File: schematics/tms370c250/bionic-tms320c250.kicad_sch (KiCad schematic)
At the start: 10 parts, among them J1 Bionic-P135, J2 Bionic-P245, U1 TMS370C250, U2 11AA010-I/TT

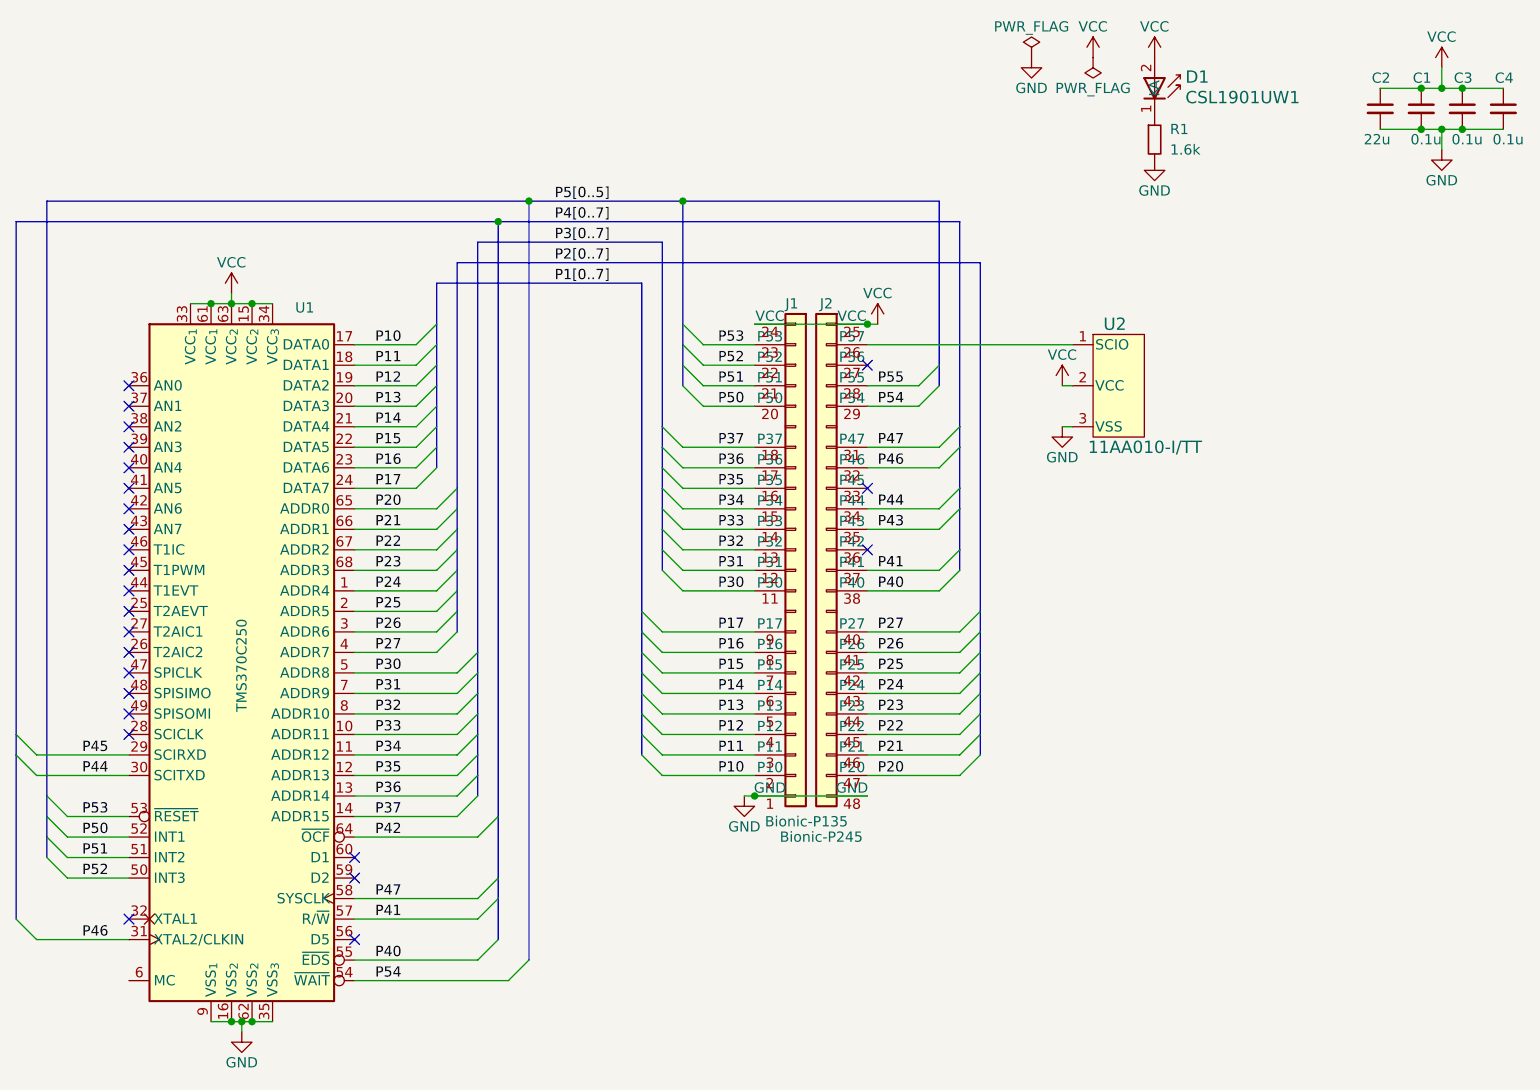
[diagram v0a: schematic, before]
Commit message: [TMS320C250] Fix missing MC and OCF connection
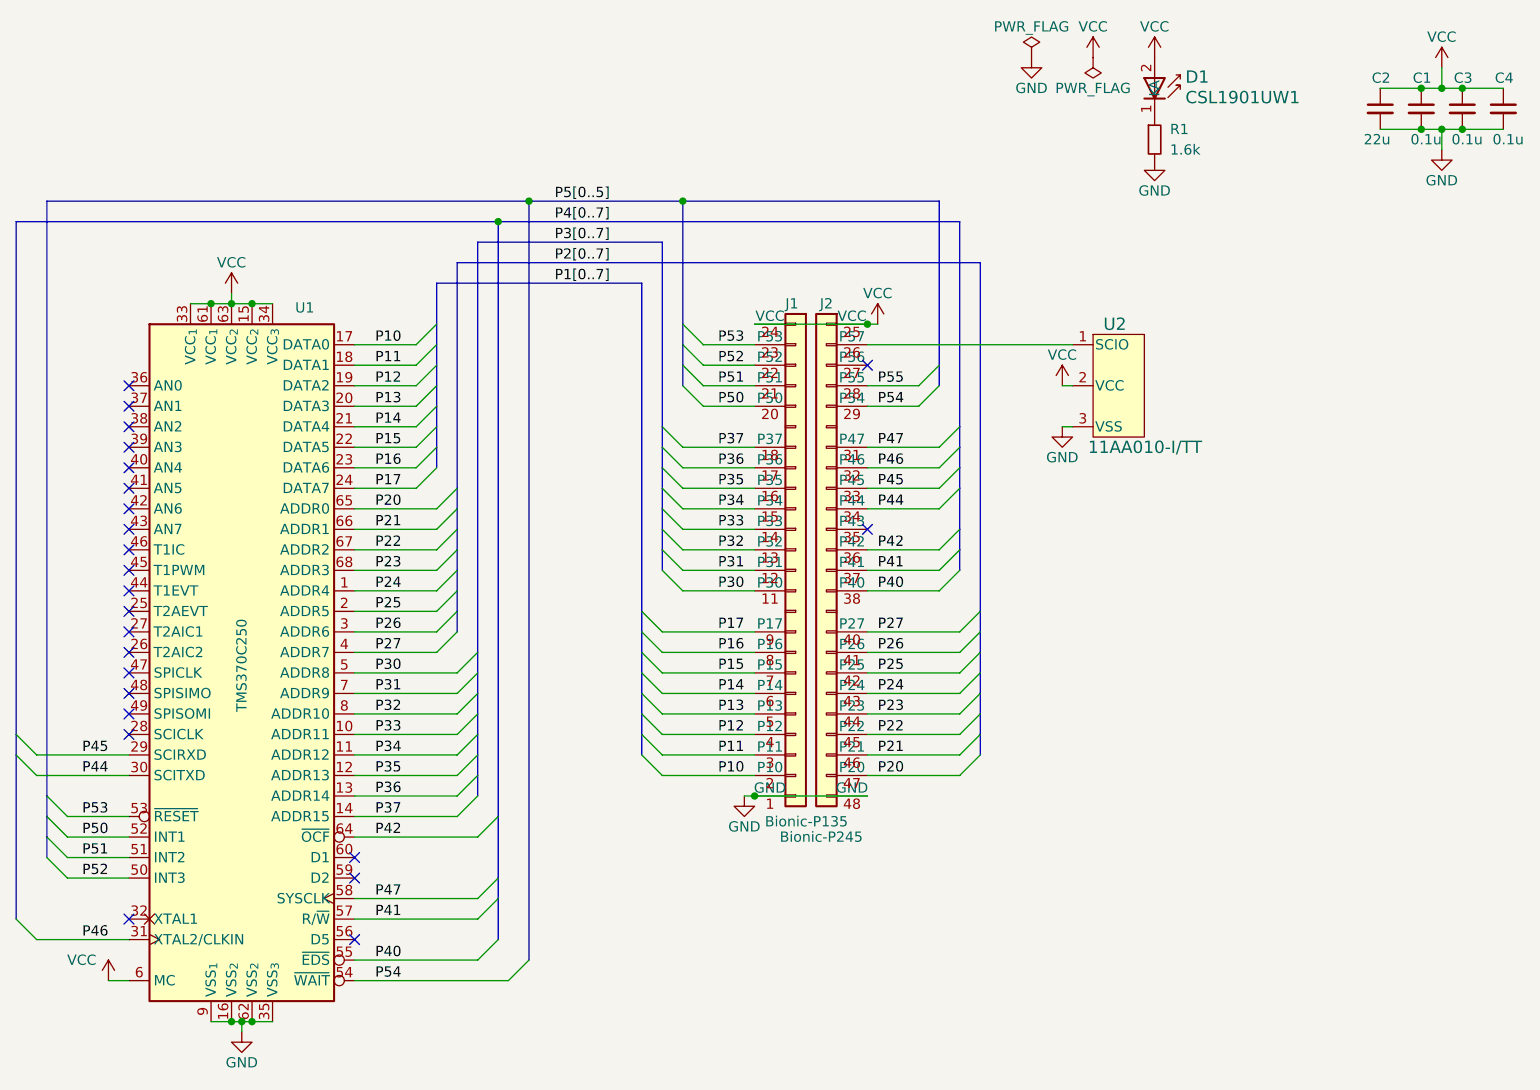
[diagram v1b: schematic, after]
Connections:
- net P42: now also J2.36 (P42)
- net P45: now also J2.33 (P45)
- net VCC: now also U1.6 (MC)
- net P43: no longer names the net of J2.35 (P43)
- no-connect marks 25 -> 24
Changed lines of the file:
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@@
 	(title_block
 		(title "BionicTMS370C250")
-		(date "2025-06-15")
-		(rev "1")
+		(date "2025-06-24")
+		(rev "2")
 		(company "Tadashi G. Takaoka")
 	)
@@
 	)
 	(no_connect
-		(at 161.29 100.33)
-	)
-	(no_connect
-		(at 161.29 92.71)
+		(at 161.29 97.79)
 	)
 	(no_connect
@@
 	)
 	(bus_entry
+		(at 172.72 90.17)
+		(size -2.54 2.54)
+		(stroke
+			(width 0)
+			(type default)
+		)
+	)
+	(bus_entry
 		(at 113.03 125.73)
 		(size -2.54 2.54)
@@
 	)
 	(bus_entry
-		(at 172.72 95.25)
-		(size -2.54 2.54)
+		(at 135.89 92.71)
+		(size 2.54 2.54)
 		(stroke
 			(width 0)
@@
 	)
 	(bus_entry
-		(at 135.89 92.71)
-		(size 2.54 2.54)
+		(at 172.72 97.79)
+		(size -2.54 2.54)
 		(stroke
 			(width 0)
@@
 		)
 	)
+	(wire
+		(pts
+			(xy 67.31 153.67) (xy 69.85 153.67)
+		)
+		(stroke
+			(width 0)
+			(type default)
+		)
+	)
 	(bus
 		(pts
@@
 		)
 	)
+	(wire
+		(pts
+			(xy 161.29 100.33) (xy 170.18 100.33)
+		)
+		(stroke
+			(width 0)
+			(type default)
+		)
+	)
 	(bus
 		(pts
@@
 	(wire
 		(pts
-			(xy 83.82 158.75) (xy 85.09 158.75)
+			(xy 161.29 92.71) (xy 170.18 92.71)
 		)
 		(stroke
@@
 	(wire
 		(pts
-			(xy 161.29 97.79) (xy 170.18 97.79)
+			(xy 83.82 158.75) (xy 85.09 158.75)
 		)
 		(stroke
@@
 	(bus
 		(pts
-			(xy 172.72 100.33) (xy 172.72 95.25)
+			(xy 172.72 100.33) (xy 172.72 97.79)
 		)
 		(stroke
@@
 	(bus
 		(pts
-			(xy 172.72 95.25) (xy 172.72 92.71)
+			(xy 172.72 92.71) (xy 172.72 97.79)
 		)
 		(stroke
@@
 	(bus
 		(pts
+			(xy 172.72 90.17) (xy 172.72 92.71)
+		)
+		(stroke
+			(width 0)
+			(type default)
+		)
+	)
+	(bus
+		(pts
 			(xy 133.35 125.73) (xy 133.35 123.19)
 		)
@@
 	(bus
 		(pts
-			(xy 172.72 87.63) (xy 172.72 92.71)
+			(xy 172.72 87.63) (xy 172.72 90.17)
 		)
 		(stroke
@@
 		)
 	)
+	(label "P45"
+		(at 162.56 92.71 0)
+		(effects
+			(font
+				(size 1.27 1.27)
+			)
+			(justify left bottom)
+		)
+	)
 	(label "P36"
 		(at 100.33 130.81 0)
@@
 		)
 	)
+	(label "P42"
+		(at 162.56 100.33 0)
+		(effects
+			(font
+				(size 1.27 1.27)
+			)
+			(justify left bottom)
+		)
+	)
 	(label "P10"
 		(at 146.05 128.27 180)
@@
 		)
 	)
-	(label "P43"
-		(at 162.56 97.79 0)
-		(effects
-			(font
-				(size 1.27 1.27)
-			)
-			(justify left bottom)
-		)
-	)
 	(label "P42"
 		(at 100.33 135.89 0)
@@
 					(unit 1)
 				)
+			)
+		)
+	)
+	(symbol
+		(lib_id "power:VCC")
+		(at 67.31 153.67 0)
+		(unit 1)
+		(exclude_from_sim no)
+		(in_bom yes)
+		(on_board yes)
+		(dnp no)
+		(property "Reference" "#PWR013"
+			(at 67.31 157.48 0)
+			(effects
+				(font
+					(size 1.27 1.27)
+				)
+				(hide yes)
+			)
+		)
+		(property "Value" "VCC"
+			(at 64.008 151.13 0)
+			(effects
+				(font
+					(size 1.27 1.27)
+				)
+			)
+		)
+		(property "Footprint" ""
+			(at 67.31 153.67 0)
+			(effects
+				(font
+					(size 1.27 1.27)
+				)
+				(hide yes)
+			)
+		)
+		(property "Datasheet" ""
+			(at 67.31 153.67 0)
+			(effects
+				(font
+					(size 1.27 1.27)
+				)
+				(hide yes)
+			)
+		)
+		(property "Description" "Power symbol creates a global label with name \"VCC\""
+			(at 67.31 153.67 0)
+			(effects
+				(font
+					(size 1.27 1.27)
+				)
+				(hide yes)
+			)
+		)
+		(pin "1"
+		)
+		(instances
+			(project "bionic-tms320c250"
+				(path "/87bdfc81-95c4-41aa-b4de-ca4774a602eb"
+					(reference "#PWR013")
+					(unit 1)
+				)
